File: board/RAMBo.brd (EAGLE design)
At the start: 104.1 x 102.9 mm, 269 parts, among them Q1 PSMN7R0-60YS, Q2 PSMN7R0-60YS, Q3 PSMN7R0-60YS, Q4 IRLML6346TRPBF, Q5 PSMN7R0-60YS, Q8 IRLML6346TRPBF, U1 ATMEGA32U2-MUR, U10 ADUM7441, U2 ATMEGA2560-16AU, U3 TPS54332DDA, U4 AD5206, U5 A4982, U6 A4982, U7 A4982, U8 A4982, U9 A4982, X1 C-GRID-02-70543, X10 C-GRID-04-70543, X11 MSTBV10, X12 SPI, X13 EXT-2, X14 C-GRID-04-70543, X15 C-GRID-04-70543, X16 32u2 EXT, X17 3x2M, X18 3x2M, X2 USB B-TH, X20 M05PTH, X21 C-GRID-03-70543, X22 C-GRID-03-70543, X23 C-GRID-03-70543, X24 C-GRID-03-70543, X25 C-GRID-03-70543, X26 C-GRID-03-70543, X27 C-GRID-02-70543, X28 C-GRID-02-70543, X29 C-GRID-02-70543, X3 C-GRID-02-70543, X30 C-GRID-02-70543, X31 M05PTH, X32 M05PTH, X33 MSTBA6, X34 PWM_EXT, X39 M05X2PTH, X4 C-GRID-04-70543, X40 Analog, X5 C-GRID-02-70543, X6 C-GRID-04-70543, X7 C-GRID-04-70543, X8 C-GRID-04-70543, X9 C-GRID-02-70543, Y1 16MHz KX-7, Y2 16MHz KX-7

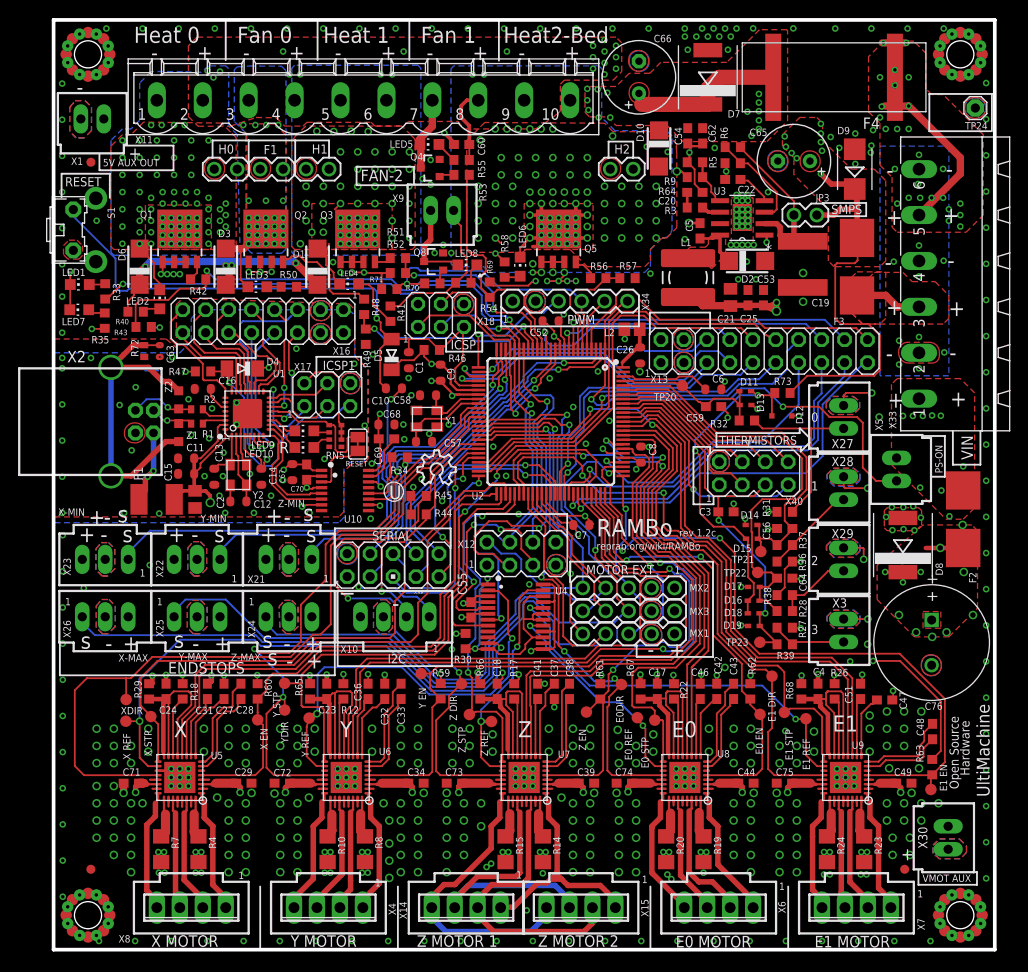
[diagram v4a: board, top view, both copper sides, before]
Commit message: move analog ext, layout changes, change vias
around mosfets, silk screen fixes, change stack up,
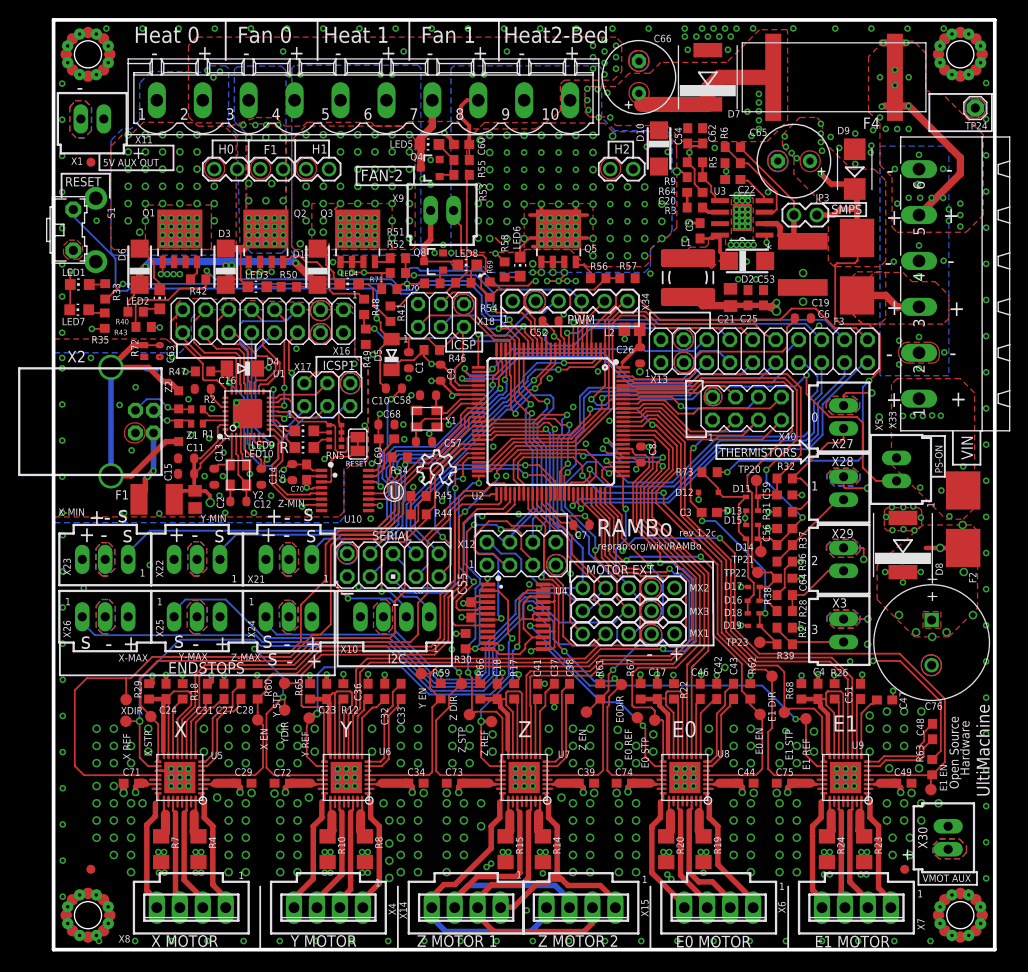
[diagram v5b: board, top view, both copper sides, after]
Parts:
- R73: value 4K7 -> 10K
- moved TP20 13.3 mm to (77.8, 51.9)
- moved C6 12.7 mm to (82.9, 69.9)
- moved C59 12.6 mm to (80.9, 50.3)
- moved R73 11.9 mm to (72.6, 52.8)
- moved D12 11.7 mm to (72.5, 50.6), turned to 180 degrees
- moved D13 11.7 mm to (77.3, 48.6), turned to 180 degrees
- moved D11 11.7 mm to (77.2, 50.1), turned to 0 degrees
- moved R32 7.66 mm to (80.9, 52.1)
- moved X40 7.21 mm to (76.7, 59.9)
- moved C3 1.84 mm to (72.6, 48.4)
- moved D15 0.06 mm to (77.3, 47.0)
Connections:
- net ADC2 renamed PF6
- net ADC4 renamed PF4
- removed net ADC3: U2.92, X40.4
- removed net ADC5: U2.94, X40.8
- new net PF3: U2.94, X40.4
- new net PF5: U2.92, X40.8
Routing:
- net ADC5: track 21.5 -> 0.00 mm
- net THERM0: track 19.1 -> 39.4 mm
- net PF5: track 0.00 -> 19.0 mm
- net OVREF: track 38.0 -> 20.5 mm, vias 2 -> 0
- net +12V2: track 158.0 -> 174.2 mm, vias 35 -> 37
- net ADC3: track 16.1 -> 0.00 mm
- net AREF: track 9.93 -> 24.2 mm
- net PF3: track 0.00 -> 13.3 mm
- net THERM3: track 45.1 -> 55.2 mm, vias 2 -> 3
- net PK0: track 25.8 -> 20.0 mm, vias 1 -> 0
- net THERM1: track 41.6 -> 47.3 mm, vias 0 -> 2
- net N$87: track 20.3 -> 14.8 mm
- net PJ7: track 32.4 -> 36.8 mm
- net PF6: track 18.2 -> 14.4 mm
- net PF4: track 18.8 -> 16.1 mm, vias 0 -> 1
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
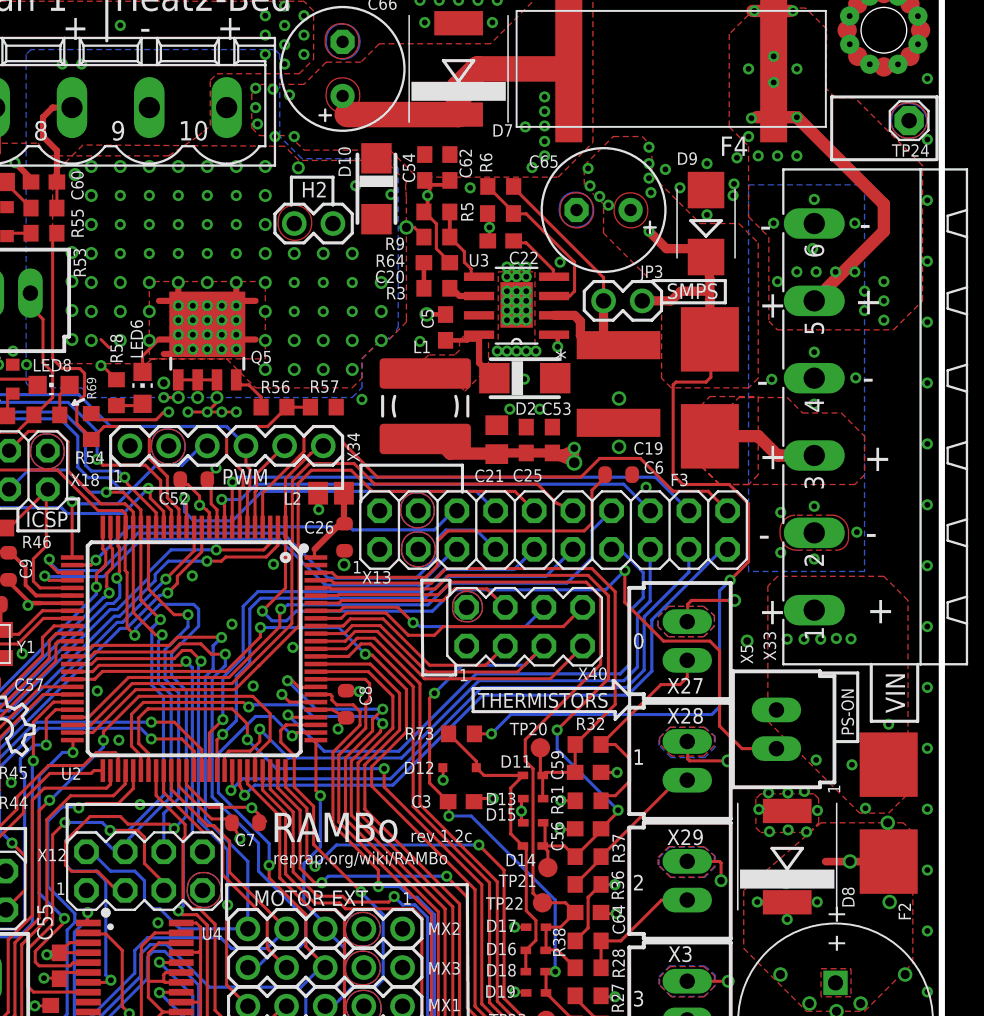
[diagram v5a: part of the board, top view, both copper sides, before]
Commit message: Change SMPS IC to LM22675, SMPS passives changed
accordingly. Shorting SMPS jumper disables SMPS. Change reverse voltage
diodes on low current rails.
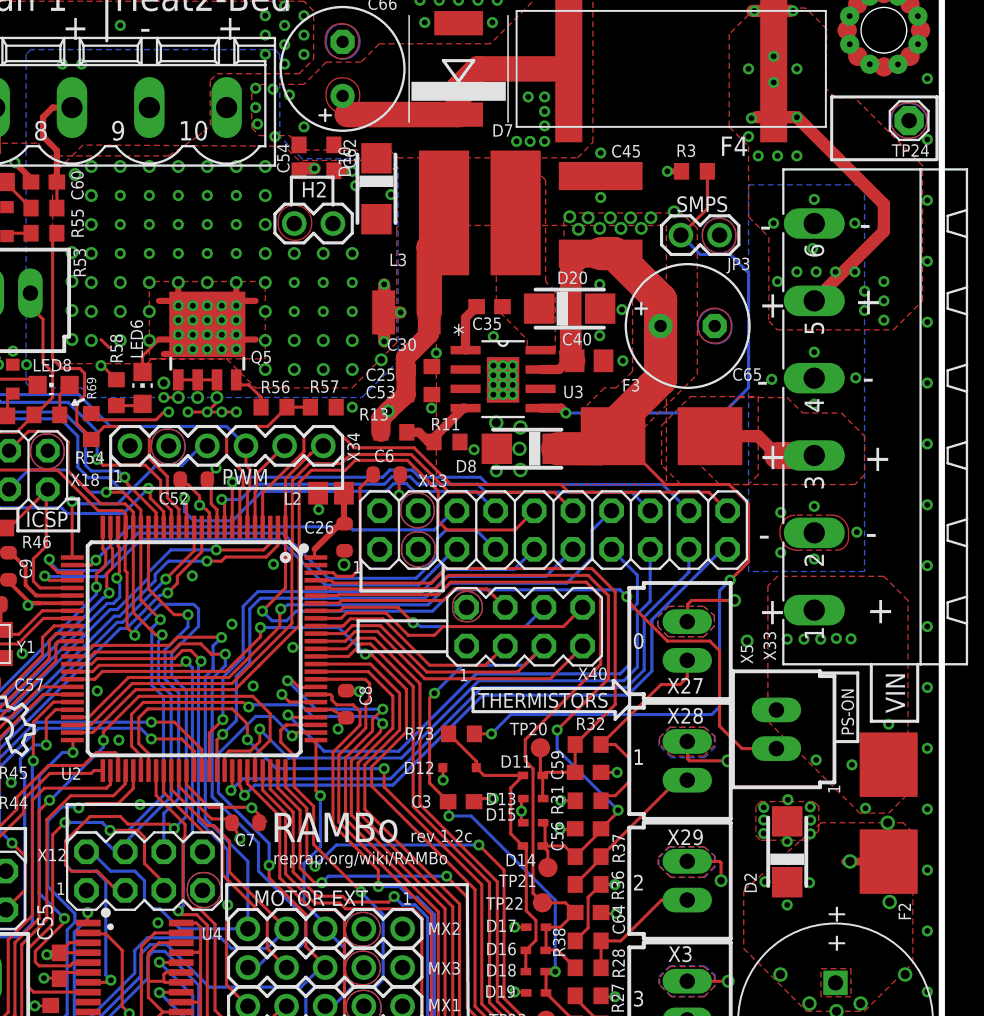
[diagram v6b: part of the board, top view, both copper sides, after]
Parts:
- removed C19: 10uF, rcl:C2220K
- removed C20: 1.8nF, rcl:C0603
- removed C21: 22uF, rcl:C0805
- removed C22: 10nF, rcl:C0603
- removed C5: 100nF, rcl:C0603
- removed D9: 1SMB5935BT3G, diode:SMB
- removed L1: 10uH, ultimachine:POWER-CHOKE_WE-TPC
- removed R5: 18K, rcl:R0603
- removed R6: 105K, rcl:R0603
- removed R64: 53.6K, rcl:R0603
- removed R9: 10K, rcl:R0603
- added C30: 10uF, resistor:C1210K
- added C35: 10nF, rcl:C0603
- added C40: 1uF, rcl:C0805
- added C45: 10uF, rcl:C2220K
- added D20: SK310A-TP, ultimachine1:SMA-SM
- added L3: 33uH, ultimachine:VLP8040
- added R11: 1K, rcl:R0603
- added R13: 2.87K, rcl:R0603
- D2: value B240A-13-F -> SK310A-TP
- D8: value S3A -> SK310A-TP; device ultimachine:DO-214AB -> ultimachine1:SMA-SM
- R3: value 18K -> 470K
- U3: value TPS54332DDA -> LM22675
- moved D2 35.6 mm to (94.0, 45.1), turned to 90 degrees
- moved D8 31.8 mm to (76.9, 71.6), turned to 180 degrees
- moved R3 18.6 mm to (87.9, 89.8), turned to 180 degrees
- moved C6 15.2 mm to (67.7, 69.9)
- moved C65 9.41 mm to (87.4, 79.6), turned to 0 degrees
- moved C53 9.26 mm to (69.8, 75.1), turned to 0 degrees
- moved C25 8.54 mm to (69.8, 77.0), turned to 0 degrees
- moved C54 8.28 mm to (61.9, 90.7)
- moved C62 7.65 mm to (64.2, 90.7)
- moved JP3 6.67 mm to (89.5, 85.6)
- moved U3 4.91 mm to (75.3, 76.1), turned to 0 degrees
- moved F3 4.49 mm to (85.7, 72.4), turned to 0 degrees
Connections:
- removed net N$111: C19.1, JP3.2, R6.2, U3.2
- removed net N$18: R3.2, U3.6
- removed net N$39: C20.1, R3.1
- removed net N$65: C5.2, D2.C, L1.1, U3.8
- removed net N$93: R64.1, R9.1, U3.5
- removed net N$94: C22.1, U3.4
- removed net N$97: R5.2, R6.1, U3.3
- new net N$131: C35.1, U3.1
- new net N$164: R11.1, R13.1, U3.4
- new net N$165: C35.2, D20.C, L3.P$1, U3.8
- net +12V: now also D2.C; no longer D8.C
- net +12V2: now also C40.1, C45.1, D8.C, R3.2, U3.7; no longer D9.C, JP3.1
- net GND: now also C30.2, C40.2, C45.2, D20.A, JP3.1, R11.2, U3.6; no longer C19.2, C20.2, C21.2, C22.2, D9.A, R5.1, R9.2, U3.7
- net N$15: now also JP3.2, R3.1, U3.5; no longer C5.1, U3.1
- net VCC: now also C30.1, L3.P$2, R13.2; no longer C21.1, L1.2, R64.2
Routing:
- net N$15: track 11.8 -> 32.4 mm, vias 2 -> 1
- net N$111: track 19.5 -> 0.00 mm
- net AREF: track 24.2 -> 9.74 mm
- net N$97: track 11.2 -> 0.00 mm
- net +12V2: track 174.2 -> 184.8 mm, vias 37 -> 39
- net N$65: track 5.63 -> 0.00 mm
- net N$93: track 5.36 -> 0.00 mm
- net N$164: track 0.00 -> 5.22 mm
- net N$94: track 3.86 -> 0.00 mm
- net +12V: track 66.5 -> 63.3 mm
- net N$131: track 0.00 -> 3.16 mm
- net VCC: track 96.4 -> 99.4 mm, vias 27 -> 25
- net PD6: track 44.3 -> 46.8 mm
- net N$18: track 2.31 -> 0.00 mm
- net PG5: track 57.0 -> 54.8 mm
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- added copper zone on layer 1, net N$165
- removed copper zone on layer 1, net N$65

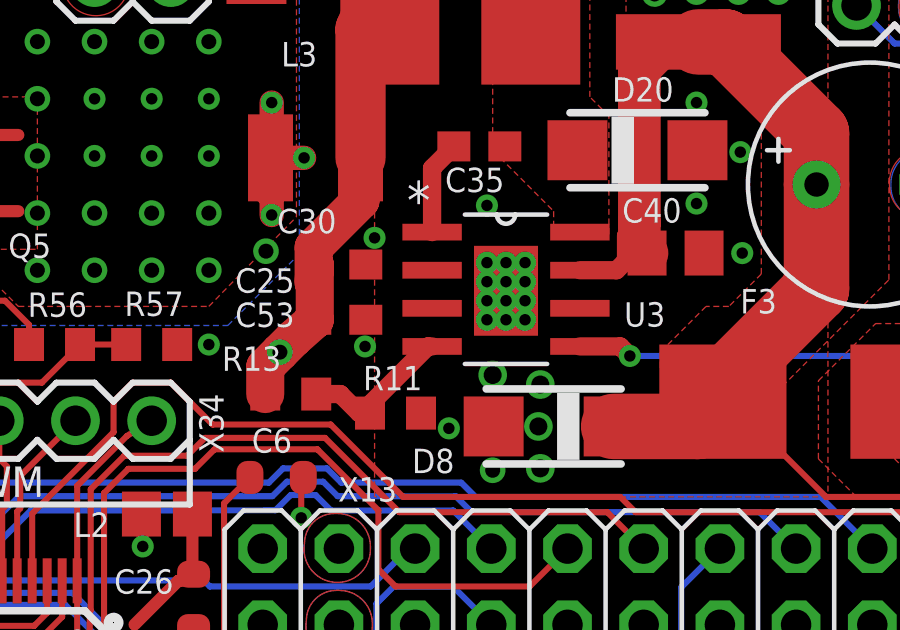
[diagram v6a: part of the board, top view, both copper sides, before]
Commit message: change SMPS to prefer 5V version of IC
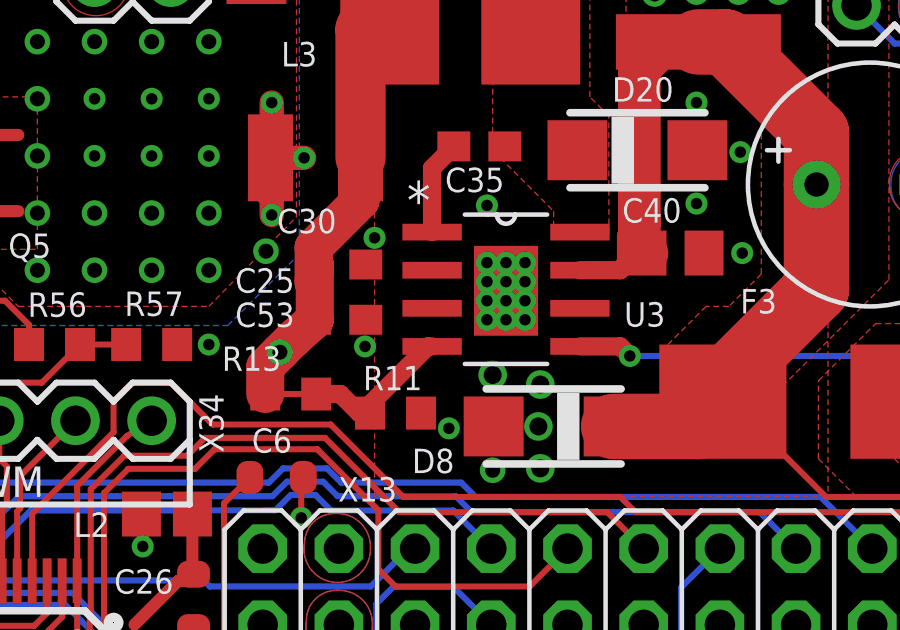
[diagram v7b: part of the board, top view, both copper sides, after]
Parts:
- R11: value 1K -> NP
- R13: value 2.87K -> NP
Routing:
- net N$164: track 5.22 -> 6.87 mm
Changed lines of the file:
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@@
 <attribute name="NAME" x="82.417" y="90.707" size="0.8128" layer="25"/>
 </element>
-<element name="R11" library="rcl" package="R0603" value="1K" x="71.628" y="72.009" smashed="yes">
+<element name="R11" library="rcl" package="R0603" value="NP" x="71.628" y="72.009" smashed="yes">
 <attribute name="NAME" x="70.5485" y="72.771" size="0.8128" layer="25"/>
 </element>
-<element name="R13" library="rcl" package="R0603" value="2.87K" x="68.1355" y="72.644" smashed="yes" rot="R180">
+<element name="R13" library="rcl" package="R0603" value="NP" x="68.1355" y="72.644" smashed="yes" rot="R180">
 <attribute name="NAME" x="67.818" y="74.2315" size="0.8128" layer="25" rot="R180"/>
 </element>
@@
 <wire x1="80.5815" y1="84.328" x2="81.671" y2="84.328" width="1.4224" layer="1"/>
 <wire x1="81.671" y1="84.328" x2="81.7245" y2="84.3815" width="1.4224" layer="1"/>
-<wire x1="77.7748" y1="76.7715" x2="78.994" y2="76.7715" width="0.6096" layer="1"/>
-<wire x1="78.994" y1="76.7715" x2="79.3115" y2="77.089" width="0.6096" layer="1"/>
-<wire x1="79.3115" y1="77.089" x2="79.3115" y2="77.9145" width="0.6096" layer="1"/>
+<wire x1="77.7748" y1="76.7715" x2="79.121" y2="76.7715" width="0.6096" layer="1"/>
+<wire x1="79.121" y1="76.7715" x2="79.3115" y2="77.0255" width="0.6096" layer="1"/>
+<wire x1="79.3115" y1="77.0255" x2="79.3115" y2="77.9145" width="0.6096" layer="1"/>
 <wire x1="79.3115" y1="77.9145" x2="79.756" y2="78.359" width="0.6096" layer="1"/>
 <wire x1="85.979" y1="69.215" x2="83.7565" y2="71.4375" width="0.2032" layer="1"/>
@@
 <wire x1="72.7075" y1="74.2315" x2="70.778" y2="72.302" width="0.6096" layer="1"/>
 <wire x1="70.778" y1="72.302" x2="70.778" y2="72.009" width="0.6096" layer="1"/>
-<wire x1="68.9855" y1="72.644" x2="69.7865" y2="72.644" width="0.6096" layer="1"/>
+<wire x1="68.9855" y1="72.644" x2="69.0245" y2="72.644" width="0.6096" layer="1"/>
+<wire x1="69.0245" y1="72.644" x2="69.7865" y2="72.644" width="0.6096" layer="1"/>
 <wire x1="69.7865" y1="72.644" x2="70.4215" y2="72.009" width="0.6096" layer="1"/>
 <wire x1="70.4215" y1="72.009" x2="70.778" y2="72.009" width="0.6096" layer="1"/>
+<wire x1="67.3735" y1="72.644" x2="69.0245" y2="72.644" width="0.2032" layer="1"/>
 </signal>
 <signal name="N$165">

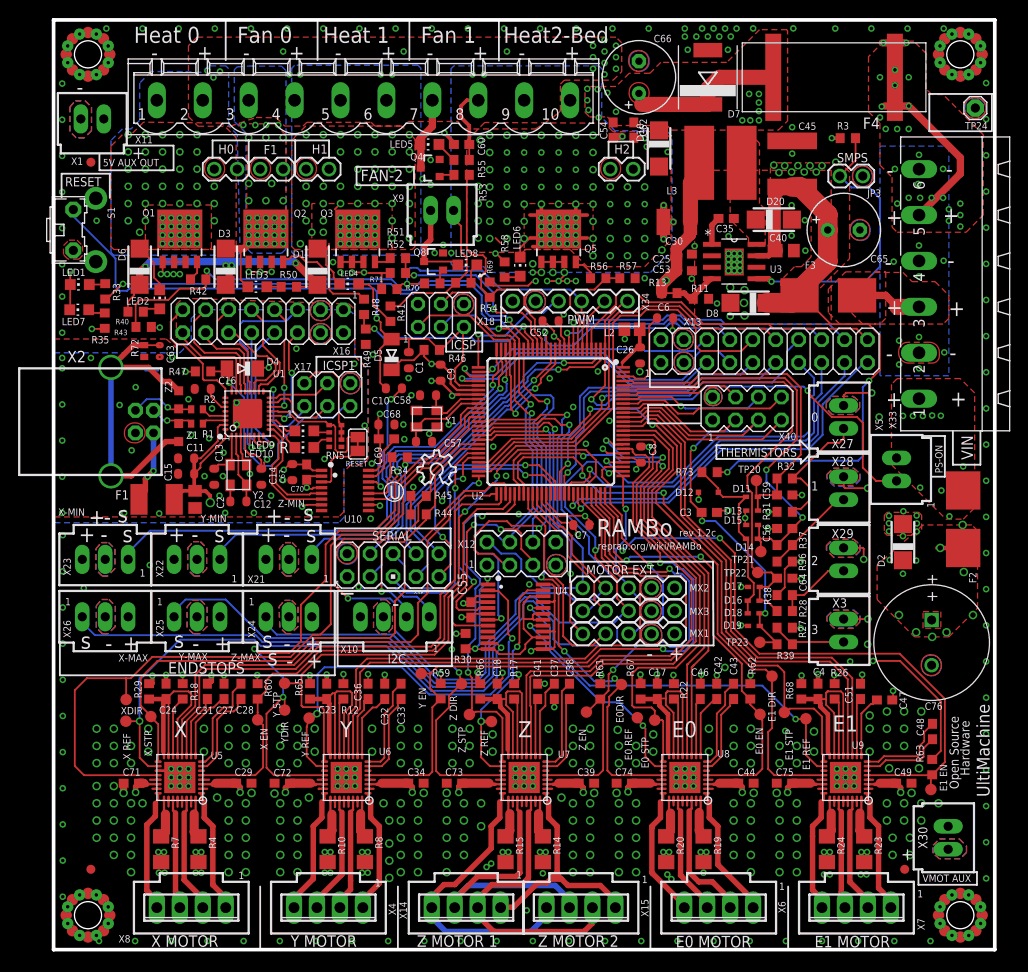
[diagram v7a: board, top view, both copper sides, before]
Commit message: rerouting split planes and adjusting isolation
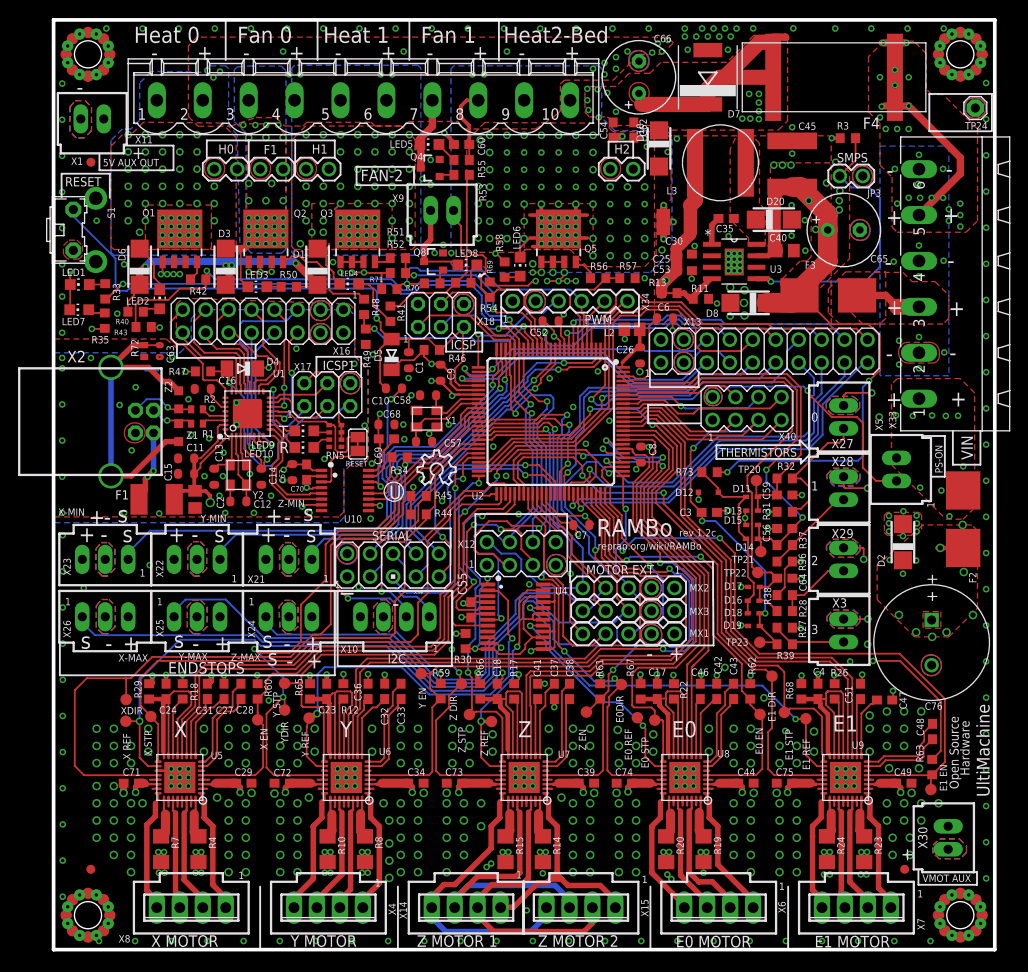
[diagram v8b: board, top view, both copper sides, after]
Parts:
- L3: device ultimachine:VLP8040 -> ultimachine:NR8040
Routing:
- net +12V3: track 57.7 -> 66.2 mm
- net GND: vias 541 -> 546
